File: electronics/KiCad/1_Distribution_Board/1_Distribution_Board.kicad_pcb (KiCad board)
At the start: 2 copper layers, 130 x 120 mm, 193 parts, among them CN1 HC-5264-3A, CN2 HC-5264-3A, J1 JST VH, J10 Generic 2.54mm, J11 Generic 2.54mm, J12 Conn_01x06, J13 Conn_01x10, J14 2.54-1*4P母, J15 2.54-1*4P母, J16 PM254V-11-06-H85, J17 Conn_02x08_Odd_Even, J18 PM254V-11-06-H85, J19 2.54-1*4P母, J2 JST VH, J20 2.54-1*4P母, J21 Jumper Pins, J22 Jumper Pins, J23 JST PH, J24 Generic 2.54mm, J25 Jumper Pins, J26 Jumper Pins, J27 JST PH, J28 Generic 2.54mm, J29 Jumper Pins, J3 JST VH, J30 Jumper Pins, J31 JST PH, J32 Generic 2.54mm, J33 Jumper Pins, J34 Jumper Pins, J35 JST PH, J36 Generic 2.54mm, J37 Jumper Pins, J38 Jumper Pins, J39 JST PH, J4 Conn_01x04, J40 Generic 2.54mm, J5 Generic 2.54mm, J6 Generic 2.54mm, J8 Generic 2.54mm, J9 Generic 2.54mm, M1 MountingHole_3.2mm_M3_ISO7380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, P1 Header-Female-2.54_1x8, P10 Header-Female-2.54_1x8, P11 Header-Female-2.54_1x2, P12 Header-Female-2.54_1x8, P13 Header-Female-2.54_1x8, P14 Header-Female-2.54_1x2, P15 Header-Female-2.54_1x8, P2 Header-Female-2.54_1x2, P3 Header-Female-2.54_1x8, P4 Header-Female-2.54_1x8, P5 Header-Female-2.54_1x2, P6 Header-Female-2.54_1x8, P7 Header-Female-2.54_1x8, P8 Header-Female-2.54_1x2, P9 Header-Female-2.54_1x8, Q1 DMG2305UX, Q2 AO3400A, Q3 AO3400A, Q4 AO3400A, Q5 AO3400A, U1 KH-2.54FH-1X20P-H8.5, U2 KH-2.54FH-1X20P-H8.5, U3 R-78C5.0-1.0, U4 R-78B12-2.0, U5 R-78B6.5-1.5, U6 PCA9306, U7 PCA9685PW, Y1 25MHz

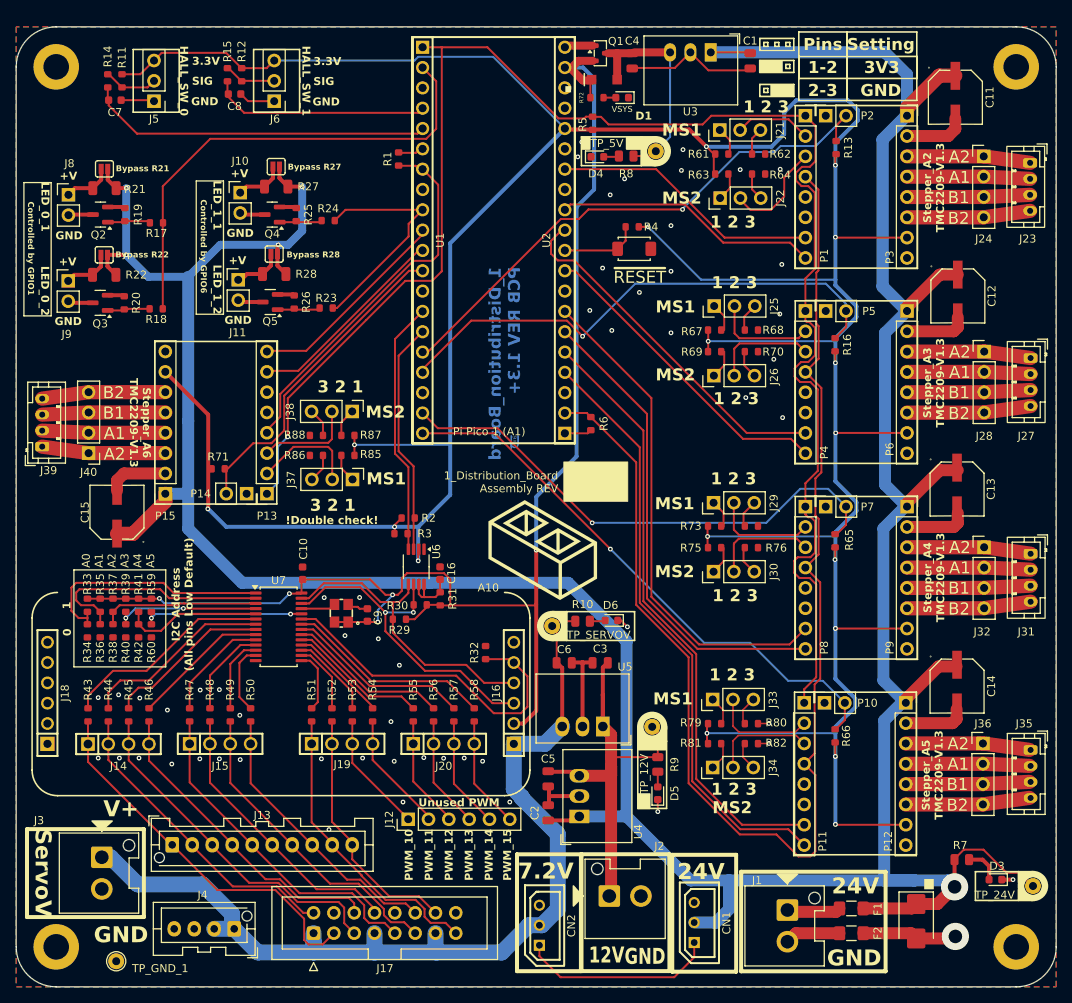
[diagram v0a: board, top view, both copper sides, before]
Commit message: distribution board v1.4: hardwired driver addresses, led ports on 24 v, no module headers, fill-only logo, rev in silkscreen
Stepper driver UART addresses are now fixed in copper:
- Removed the ten MS1/MS2 jumper headers (J21, J22, J25, J26, J29, J30,
  J33, J34, J37, J38) and the twenty 10k resistors that served only them
  (R61-R64, R67-R70, R73-R76, R79-R82, R85-R88). The DIAG pull-ups R13,
  R16, R65, R66 and R71 stay, and so does R72, the series resistor of
  the VSYS LED D7.
- Each driver's MS1 (AD0) and MS2 (AD1) pins are tied straight to GND or
  +3V3 through new sheet pins on the root sheet: A2 = 0, A3 = 1, A4 = 2,
  A5 = 3 on UART0 and A6 = 0 on UART1. This is the address map the
  firmware already uses (TMC_UART_ADDRESSES), so firmware does not change.
- On the board the low pins join the ground pour, two of them through a
  short ground stitch and via, and the high pins get short bottom-layer
  +3V3 tracks. Tracks and vias that only served the jumpers are removed.
- Removed the jumper silkscreen: the Pins/Setting legend, the "1 2 3" and
  "3 2 1" pin numbers, the MS1/MS2 labels and "!Double check!".
- The Stepper_Module sheet loses its jumper block and microstep table; a
  note on the root sheet gives the address map.

LED and fan ports run straight from 24 V:
- Removed the 180 ohm resistors R21, R22, R27, R28 and the bypass solder
  jumpers JP1-JP4. Pin 1 of J8, J9, J10 and J11 now connects directly to
  +24V, the state v1.3 boards were built in with the bypasses bridged.
- Removed the four "Bypass Rxx" labels.

Plug-in PCA9685 module headers removed:
- Removed J14, J15, J16, J18, J19 and J20, the module's silkscreen outline,
  the "A10" label and the three tracks that only went to J16. A new ground
  via replaces J16's ground pin as the stitch for that patch of ground pour.
- The on-board PCA9685 (U7) and everything it uses stay, including the
  220 ohm output resistors R43-R58 on the path to J17 and J12.

Oscillator follow-ups:
- D1 (MBR120VLSFT1G, LC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
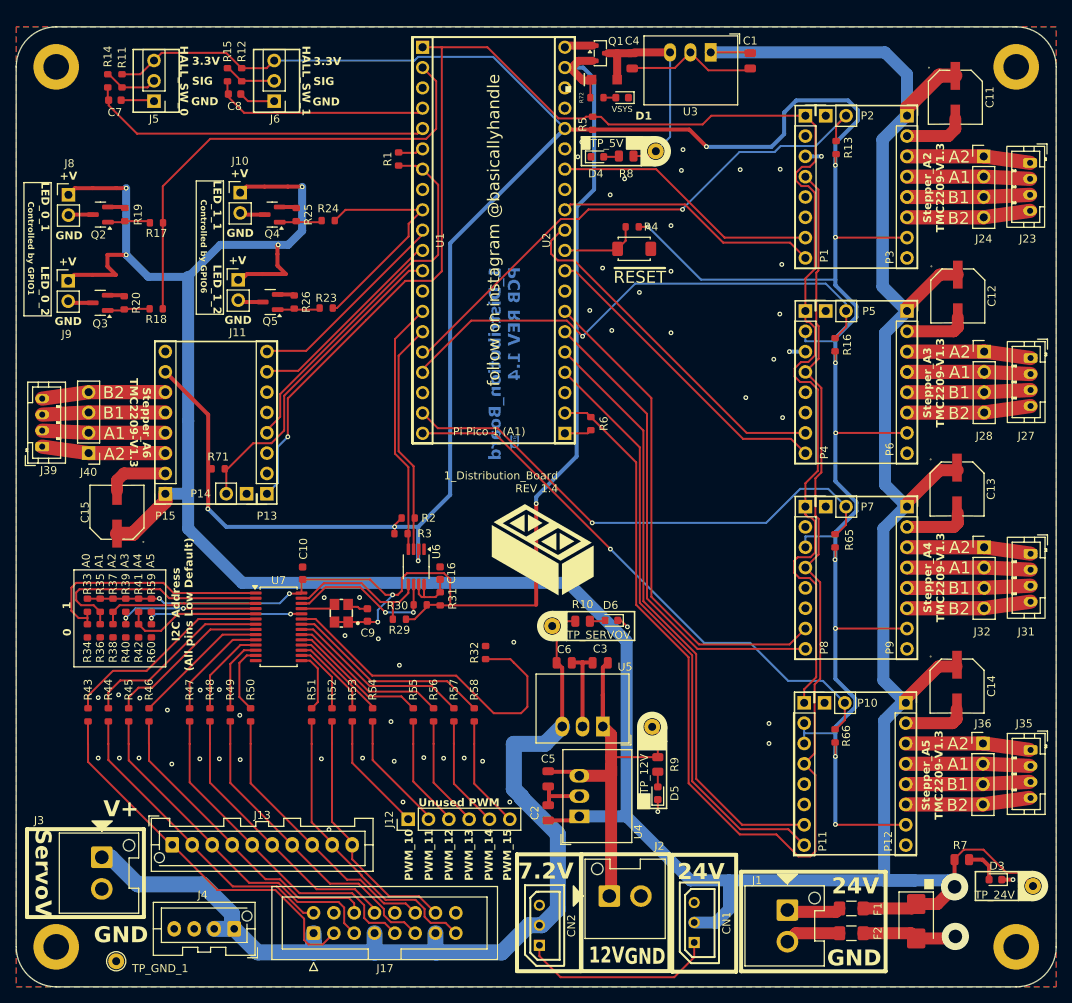
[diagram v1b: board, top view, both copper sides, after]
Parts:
- removed J14, J15, J19, J20: 2.54-1*4P母, EasyEDA:HDR-TH_4P-P2.54-V-F
- removed J16, J18: PM254V-11-06-H85, EasyEDA:HDR-TH_6P-P2.54-V-F
- removed J21, J22, J25, J26, J29, J30, J33, J34, J37, J38: Jumper Pins, Connector_PinHeader_2.54mm:PinHeader_1x03_P2.54mm_Vertical
- removed JP1, JP2, JP3, JP4: ~, PCM_SparkFun-Jumper:Jumper_2_NO
- removed R21, R22, R27, R28: 180Ω, PCM_JLCPCB:R_1206
- removed R61, R62, R63, R64, R67, R68, R69, R70, R73, R74, R75, R76, R79, R80, R81, R82, R85, R86, R87, R88: 10kΩ, PCM_JLCPCB:R_0603
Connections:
- J10 pad 1: Net-(J10-Pin_1) -> +24V
- J11 pad 1: Net-(J11-Pin_1) -> +24V
- J8 pad 1: Net-(J8-Pin_1) -> +24V
- J9 pad 1: Net-(J9-Pin_1) -> +24V
- P1 pad 2: /Stepper Module/MS1 -> GND
- P1 pad 3: /Stepper Module/MS2 -> GND
- P10 pad 2: /Stepper Module3/MS1 -> +3V3
- P10 pad 3: /Stepper Module3/MS2 -> +3V3
- P13 pad 2: /Stepper Module4/MS1 -> GND
- P13 pad 3: /Stepper Module4/MS2 -> GND
- P4 pad 2: /Stepper Module1/MS1 -> +3V3
- P4 pad 3: /Stepper Module1/MS2 -> GND
- P7 pad 2: /Stepper Module2/MS1 -> GND
- P7 pad 3: /Stepper Module2/MS2 -> +3V3
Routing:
- net +3V3: track 456.8 -> 399.6 mm, vias 17 -> 13
- net /PCA9685 Module/I2C0_SCL_5V: track 42.1 -> 19.6 mm
- net /PCA9685 Module/I2C0_SDA_5V: track 38.3 -> 18.8 mm
- net +24V: track 451.8 -> 471.2 mm
- net /Stepper Module4/MS1: track 13.3 -> 0.00 mm
- net /Stepper Module2/MS2: track 13.2 -> 0.00 mm
- net /Stepper Module2/MS1: track 13.1 -> 0.00 mm
- net /Stepper Module3/MS1: track 13.0 -> 0.00 mm
- net /Stepper Module1/MS2: track 13.0 -> 0.00 mm
- net /Stepper Module1/MS1: track 12.9 -> 0.00 mm
- net /Stepper Module3/MS2: track 12.9 -> 0.00 mm
- net /Stepper Module/MS2: track 12.8 -> 0.00 mm
- net /Stepper Module4/MS2: track 12.3 -> 0.00 mm
- net VSYS: track 174.2 -> 163.0 mm
- net /Stepper Module/MS1: track 9.58 -> 0.00 mm
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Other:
- board text added: "1_Distribution_Board PCB REV 1.4"
- board text added: "1_Distribution_Board REV 1.4"
- board text added: "follow on instagram @basicallyhandle"
- board text removed: "!Double check!"
- board text removed: "1 2 3"
- board text removed: "1-2"
- board text removed: "1_Distribution_Board Assembly REV"
- board text removed: "1_Distribution_Board PCB REV 1.3+"
- board text removed: "2-3"
- board text removed: "3 2 1"
- board text removed: "3V3"
- board text removed: "A10"
- board text removed: "Bypass R21"
- board text removed: "Bypass R22"
- board text removed: "Bypass R27"
- board text removed: "Bypass R28"
- board text removed: "MS1"
- board text removed: "MS2"
- board text removed: "Pins"
- board text removed: "Setting"

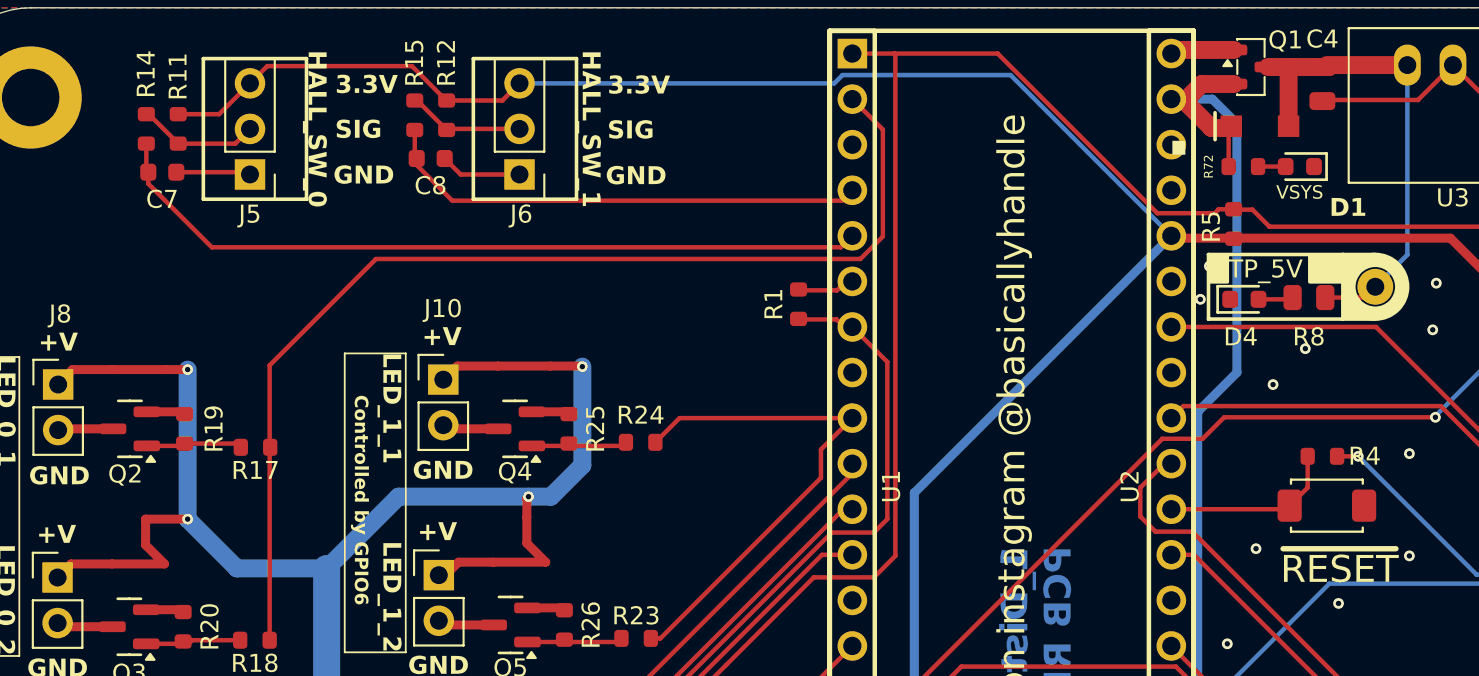
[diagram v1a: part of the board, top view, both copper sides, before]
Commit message: distribution board v1.4: square corners on the j9 and j11 24 v feeds, d1 and d7 labels at their parts
Two layout and silkscreen fixes from review:

- The +24V feeds to LED ports J9 and J11 ran down from their vias at
  45 degrees into the old R22 and R28 pad points and then turned straight
  back along the port track, leaving a 45-degree notch between two tracks
  of the same net, the kind of acute angle fab checks flag. Each feed now
  runs straight down and turns 90 degrees into the port track, and the
  two diagonal segments are gone. Nets, widths and the vias are unchanged.
- D1, the diode that is now fitted, had no label of its own: the only
  "D1" on the silkscreen was a free text beside the VSYS LED D7. D1's
  reference now sits on the silkscreen right of the diode, and D7's
  reference takes the old spot beside its VSYS label.

DRC with refilled zones and schematic parity reports the same items as
before, ERC and the schematic netlist are unchanged, and no pad or via
changes net.

Co-Authored-By: Claude Opus 5.5 (1M context) <noreply@anthropic.com>
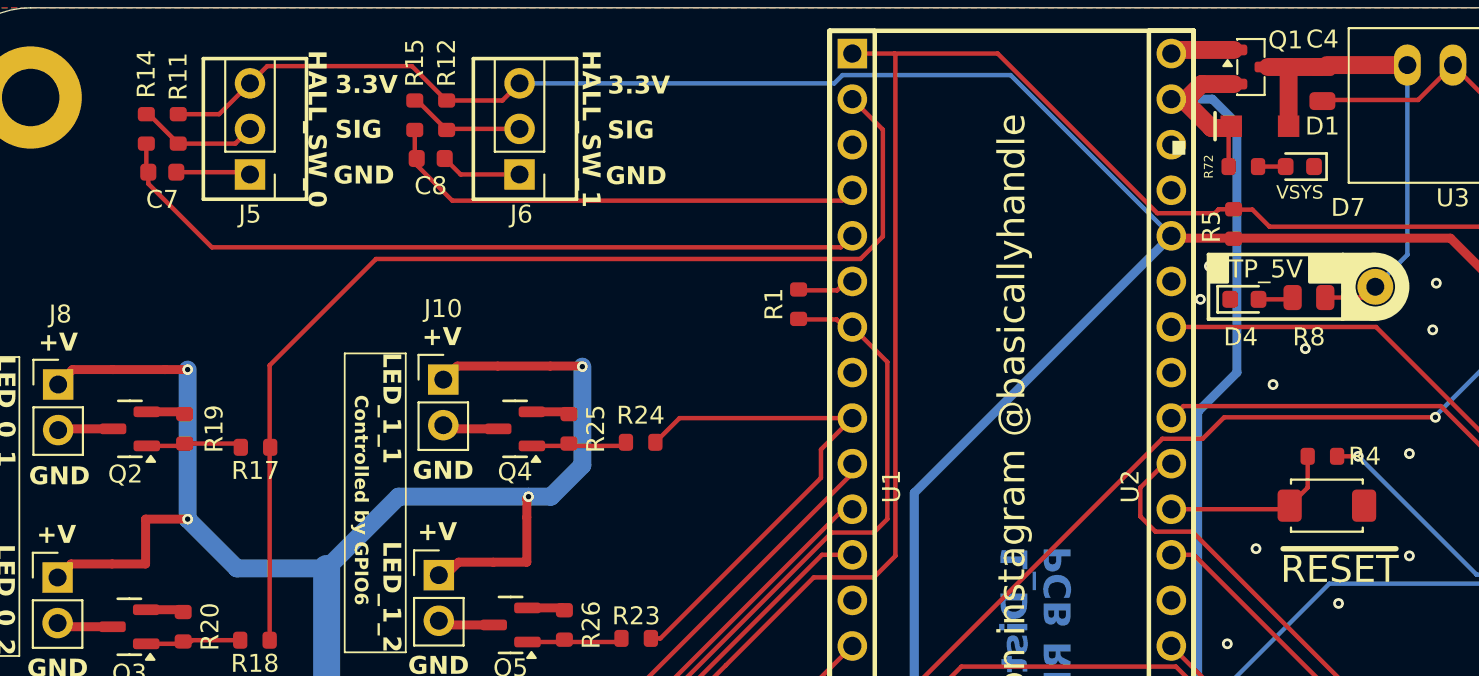
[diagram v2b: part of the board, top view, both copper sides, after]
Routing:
- net +24V: track 471.2 -> 468.2 mm
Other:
- board text removed: "D1"
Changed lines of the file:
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@@
 		(tags "LED")
 		(property "Reference" "D7"
-			(at 0 -1.43 0)
+			(at -2.6924 -2.286 0)
 			(layer "F.SilkS")
-			(hide yes)
 			(effects
 				(font
@@
 		(tags "SparkFun SOD-123 Diode")
 		(property "Reference" "D1"
-			(at 0 -1.5 0)
-			(layer "F.Fab")
+			(at 3.4828 0 0)
+			(layer "F.SilkS")
 			(effects
 				(font
-					(size 0.5 0.5)
-					(thickness 0.1)
+					(size 1 1)
+					(thickness 0.15)
 				)
 			)
@@
 		)
 	)
-	(gr_text "D1"
-		(at 103.4352 36.1356 0)
-		(layer "F.SilkS")
-		(effects
-			(font
-				(size 1 1)
-				(thickness 0.15)
-				(bold yes)
-			)
-		)
-	)
 	(gr_text "TP_SERVOV"
 		(at 93.8 101.6 0)
@@
 	(segment
 		(start 57.6564 53.4)
-		(end 57.6564 54.8464)
+		(end 57.6564 55.9)
 		(width 0.5)
 		(layer "F.Cu")
@@
 	(segment
 		(start 36.4064 53.5)
-		(end 36.4064 54.9464)
+		(end 36.4064 56)
 		(width 0.5)
 		(layer "F.Cu")
@@
 	)
 	(segment
-		(start 36.4064 54.9464)
-		(end 37.46 56)
-		(width 0.5)
-		(layer "F.Cu")
-		(net "+24V")
-	)
-	(segment
 		(start 136.35 84.521)
 		(end 140.446 80.425)
@@
 	(segment
 		(start 55.79 55.9)
-		(end 58.71 55.9)
+		(end 57.6564 55.9)
 		(width 0.5)
 		(layer "F.Cu")
@@
 	(segment
 		(start 34.54 56)
-		(end 37.46 56)
+		(end 36.4064 56)
 		(width 0.5)
 		(layer "F.Cu")
@@
 		(layer "F.Cu")
 		(net "+24V")
-	)
-	(segment
-		(start 57.6564 54.8464)
-		(end 58.71 55.9)
-		(width 0.5)
-		(layer "F.Cu")
-		(net "+24V")
